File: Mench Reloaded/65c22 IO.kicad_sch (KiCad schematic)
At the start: 6 parts, among them J6 VIA1 Port A, J7 Int Sel 1, J8 VIA1 Port B, U4 W65C22SxP

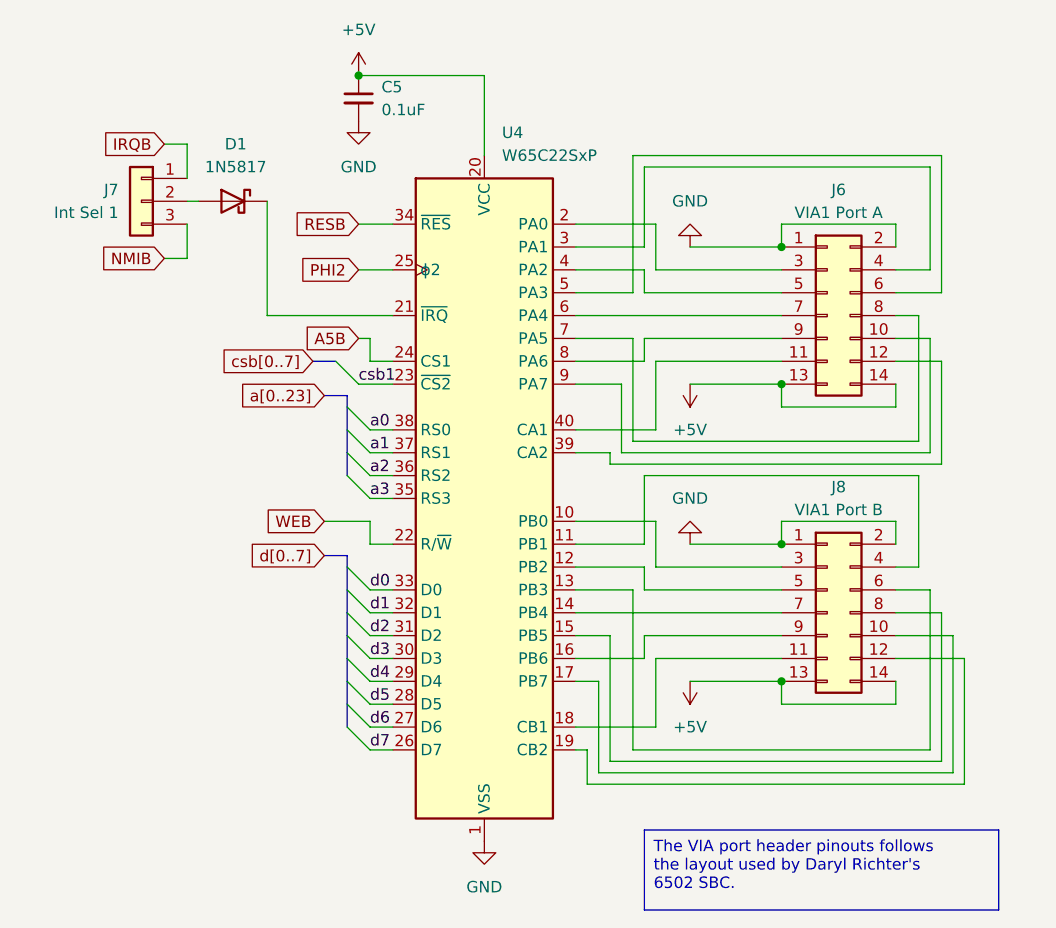
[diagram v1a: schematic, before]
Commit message: Completed all traces. Added a Zif socket footprint to ensure one will fit. Added a solder jumper for RAM options.
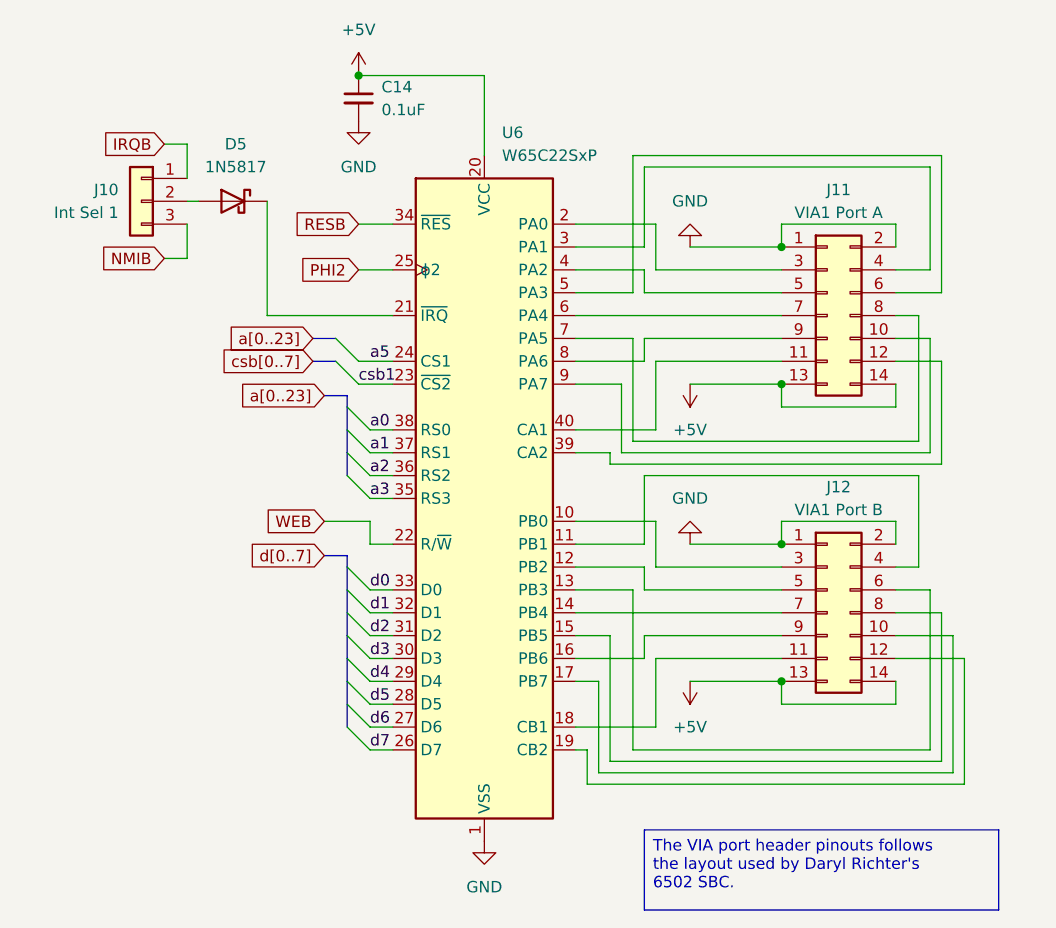
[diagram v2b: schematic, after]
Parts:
- renumbered C5 to C14, D1 to D5, J7 to J10, J6 to J11, J8 to J12, U4 to U6
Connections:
- net A5B renamed a5

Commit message: Added power selector header (ftdi vs battery). Added 128kB vs 256kB RAM selector. Added pull up for RESB and DS1813. Reworked traces at top of the board using streets and avenues.
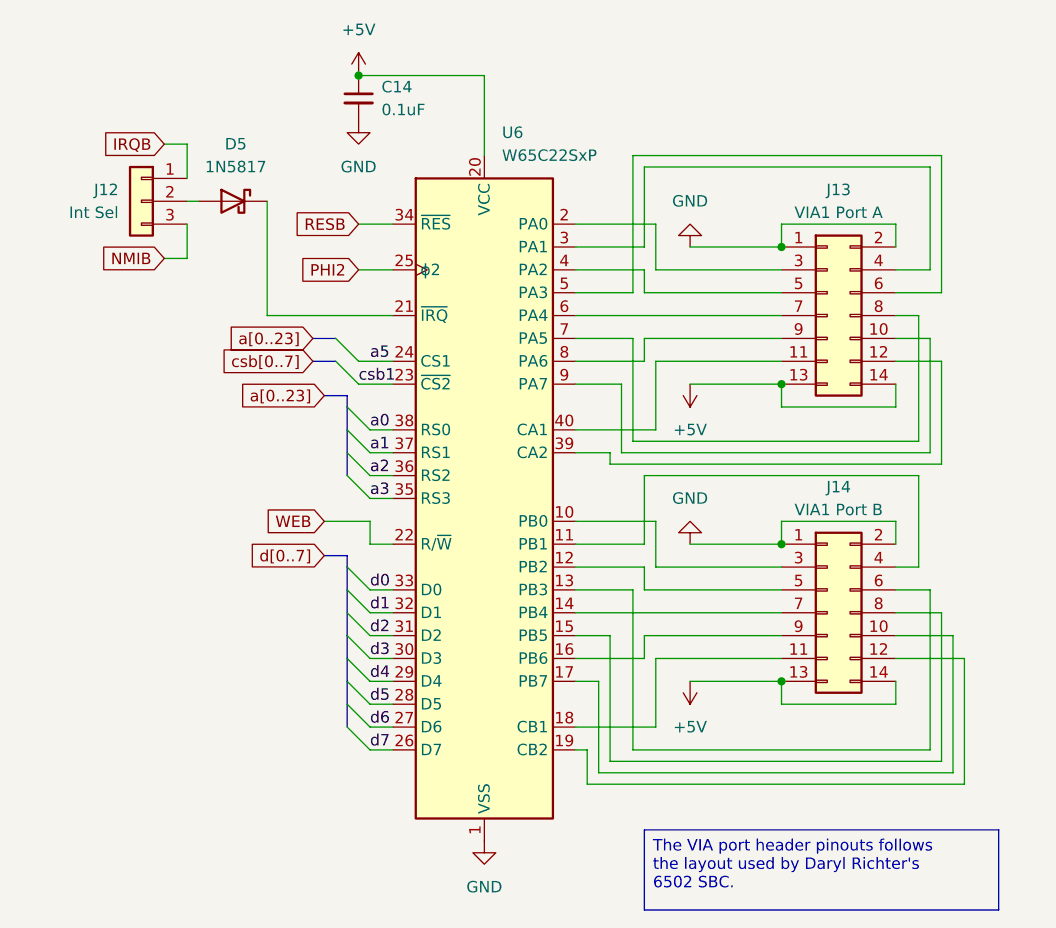
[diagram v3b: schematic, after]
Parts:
- J12: renamed from J10; value Int Sel 1 -> Int Sel
- renumbered J11 to J13, J12 to J14
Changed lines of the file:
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@@
 		(dnp no)
 		(fields_autoplaced yes)
-		(property "Reference" "J11"
+		(property "Reference" "J13"
 			(at 119.38 45.72 0)
 			(effects
@@
 			(project "Mench Reloaded"
 				(path "/e63e39d7-6ac0-4ffd-8aa3-1841a4541b55/beeb26c7-6cc0-46cc-a13d-dae16fc6429a"
-					(reference "J11")
+					(reference "J13")
 					(unit 1)
 				)
@@
 		(on_board yes)
 		(dnp no)
-		(property "Reference" "#PWR041"
+		(property "Reference" "#PWR042"
 			(at 102.87 63.5 0)
 			(effects
@@
 			(project "Mench Reloaded"
 				(path "/e63e39d7-6ac0-4ffd-8aa3-1841a4541b55/beeb26c7-6cc0-46cc-a13d-dae16fc6429a"
-					(reference "#PWR041")
+					(reference "#PWR042")
 					(unit 1)
 				)
@@
 		(dnp no)
 		(fields_autoplaced yes)
-		(property "Reference" "#PWR039"
+		(property "Reference" "#PWR040"
 			(at 80.01 124.46 0)
 			(effects
@@
 			(project "Mench Reloaded"
 				(path "/e63e39d7-6ac0-4ffd-8aa3-1841a4541b55/beeb26c7-6cc0-46cc-a13d-dae16fc6429a"
-					(reference "#PWR039")
+					(reference "#PWR040")
 					(unit 1)
 				)
@@
 		(on_board yes)
 		(dnp no)
-		(property "Reference" "#PWR040"
+		(property "Reference" "#PWR041"
 			(at 102.87 45.72 0)
 			(effects
@@
 			(project "Mench Reloaded"
 				(path "/e63e39d7-6ac0-4ffd-8aa3-1841a4541b55/beeb26c7-6cc0-46cc-a13d-dae16fc6429a"
-					(reference "#PWR040")
+					(reference "#PWR041")
 					(unit 1)
 				)
@@
 		(dnp no)
 		(fields_autoplaced yes)
-		(property "Reference" "J12"
+		(property "Reference" "J14"
 			(at 119.38 78.74 0)
 			(effects
@@
 			(project "Mench Reloaded"
 				(path "/e63e39d7-6ac0-4ffd-8aa3-1841a4541b55/beeb26c7-6cc0-46cc-a13d-dae16fc6429a"
-					(reference "J12")
+					(reference "J14")
 					(unit 1)
 				)
@@
 		(dnp no)
 		(fields_autoplaced yes)
-		(property "Reference" "#PWR038"
+		(property "Reference" "#PWR039"
 			(at 66.04 44.45 0)
 			(effects
@@
 			(project "Mench Reloaded"
 				(path "/e63e39d7-6ac0-4ffd-8aa3-1841a4541b55/beeb26c7-6cc0-46cc-a13d-dae16fc6429a"
-					(reference "#PWR038")
+					(reference "#PWR039")
 					(unit 1)
 				)
@@
 		(on_board yes)
 		(dnp no)
-		(property "Reference" "#PWR043"
+		(property "Reference" "#PWR044"
 			(at 102.87 96.52 0)
 			(effects
@@
 			(project "Mench Reloaded"
 				(path "/e63e39d7-6ac0-4ffd-8aa3-1841a4541b55/beeb26c7-6cc0-46cc-a13d-dae16fc6429a"
-					(reference "#PWR043")
+					(reference "#PWR044")
 					(unit 1)
 				)
@@
 		(on_board yes)
 		(dnp no)
-		(property "Reference" "J10"
+		(property "Reference" "J12"
 			(at 39.37 45.72 0)
 			(effects
@@
 			)
 		)
-		(property "Value" "Int Sel 1"
+		(property "Value" "Int Sel"
 			(at 39.37 48.26 0)
 			(effects
@@
 			(project "Mench Reloaded"
 				(path "/e63e39d7-6ac0-4ffd-8aa3-1841a4541b55/beeb26c7-6cc0-46cc-a13d-dae16fc6429a"
-					(reference "J10")
+					(reference "J12")
 					(unit 1)
 				)
@@
 		(on_board yes)
 		(dnp no)
-		(property "Reference" "#PWR042"
+		(property "Reference" "#PWR043"
 			(at 102.87 78.74 0)
 			(effects
@@
 			(project "Mench Reloaded"
 				(path "/e63e39d7-6ac0-4ffd-8aa3-1841a4541b55/beeb26c7-6cc0-46cc-a13d-dae16fc6429a"
-					(reference "#PWR042")
+					(reference "#PWR043")
 					(unit 1)
 				)
@@
 		(dnp no)
 		(fields_autoplaced yes)
-		(property "Reference" "#PWR037"
+		(property "Reference" "#PWR038"
 			(at 66.04 36.83 0)
 			(effects
@@
 			(project "Mench Reloaded"
 				(path "/e63e39d7-6ac0-4ffd-8aa3-1841a4541b55/beeb26c7-6cc0-46cc-a13d-dae16fc6429a"
-					(reference "#PWR037")
-					(unit 1)
-				)
+					(reference "#PWR038")
+					(unit 1)
+				)

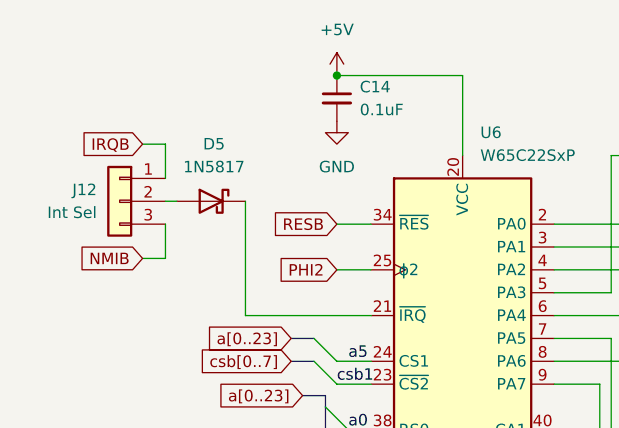
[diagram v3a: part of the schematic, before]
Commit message: Moved EEPROM North to create more space for traces. Reworked all traces from CPU to fix rats nest wiring. Added LED to csb2 to allow for debugging when internal bus is used. Added to list of signal net classes to make consistant data traces.
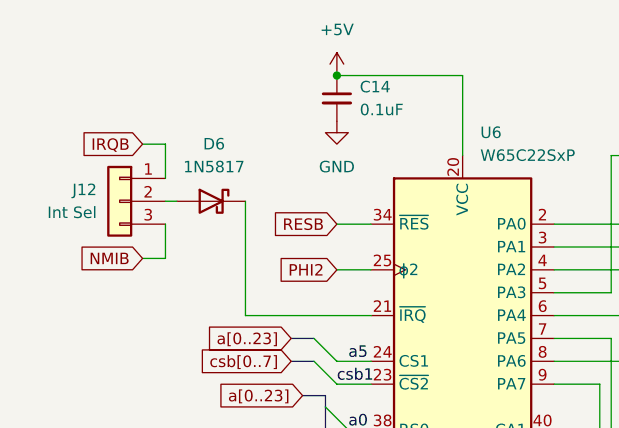
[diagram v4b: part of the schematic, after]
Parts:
- renumbered D5 to D6
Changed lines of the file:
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@@
 		(dnp no)
 		(fields_autoplaced yes)
-		(property "Reference" "D5"
+		(property "Reference" "D6"
 			(at 52.3875 40.64 0)
 			(effects
@@
 			(project "Mench Reloaded"
 				(path "/e63e39d7-6ac0-4ffd-8aa3-1841a4541b55/beeb26c7-6cc0-46cc-a13d-dae16fc6429a"
-					(reference "D5")
+					(reference "D6")
 					(unit 1)
 				)
